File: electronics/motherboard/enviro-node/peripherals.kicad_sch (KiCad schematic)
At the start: 11 parts, among them J5 ST1W008S4AR1500, J6 2604-3105, Q3 BSS214NW, U3 TCA9534

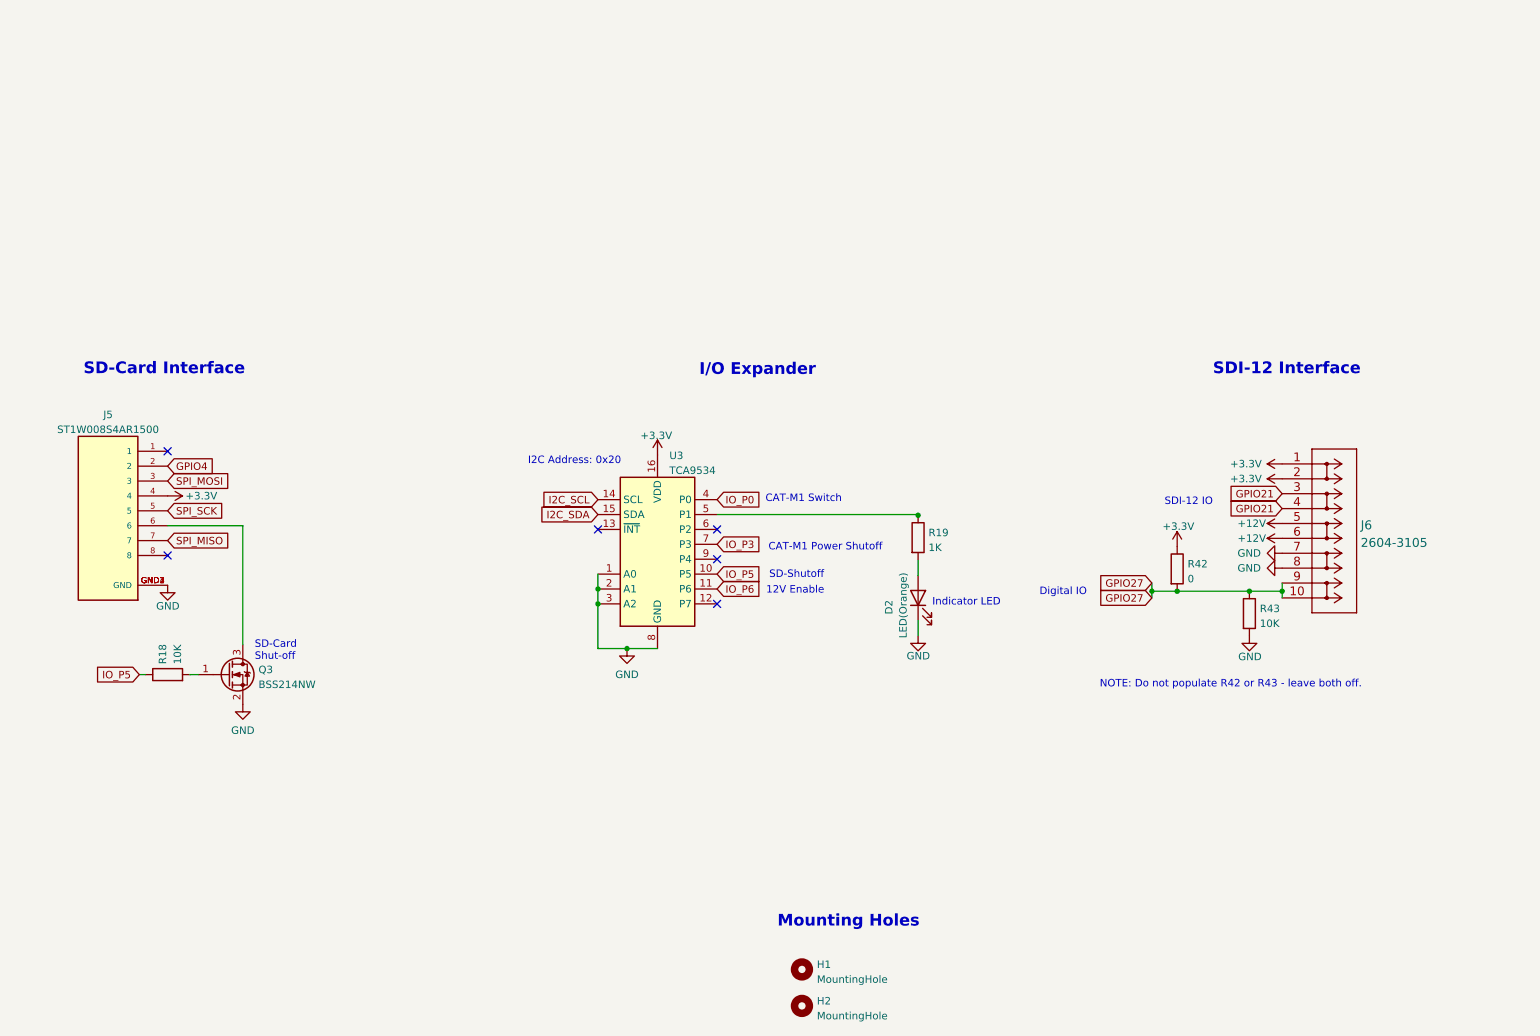
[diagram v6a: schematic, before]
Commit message: v1.0.3, added TMP1075 temp sensor, now using kicad 8.
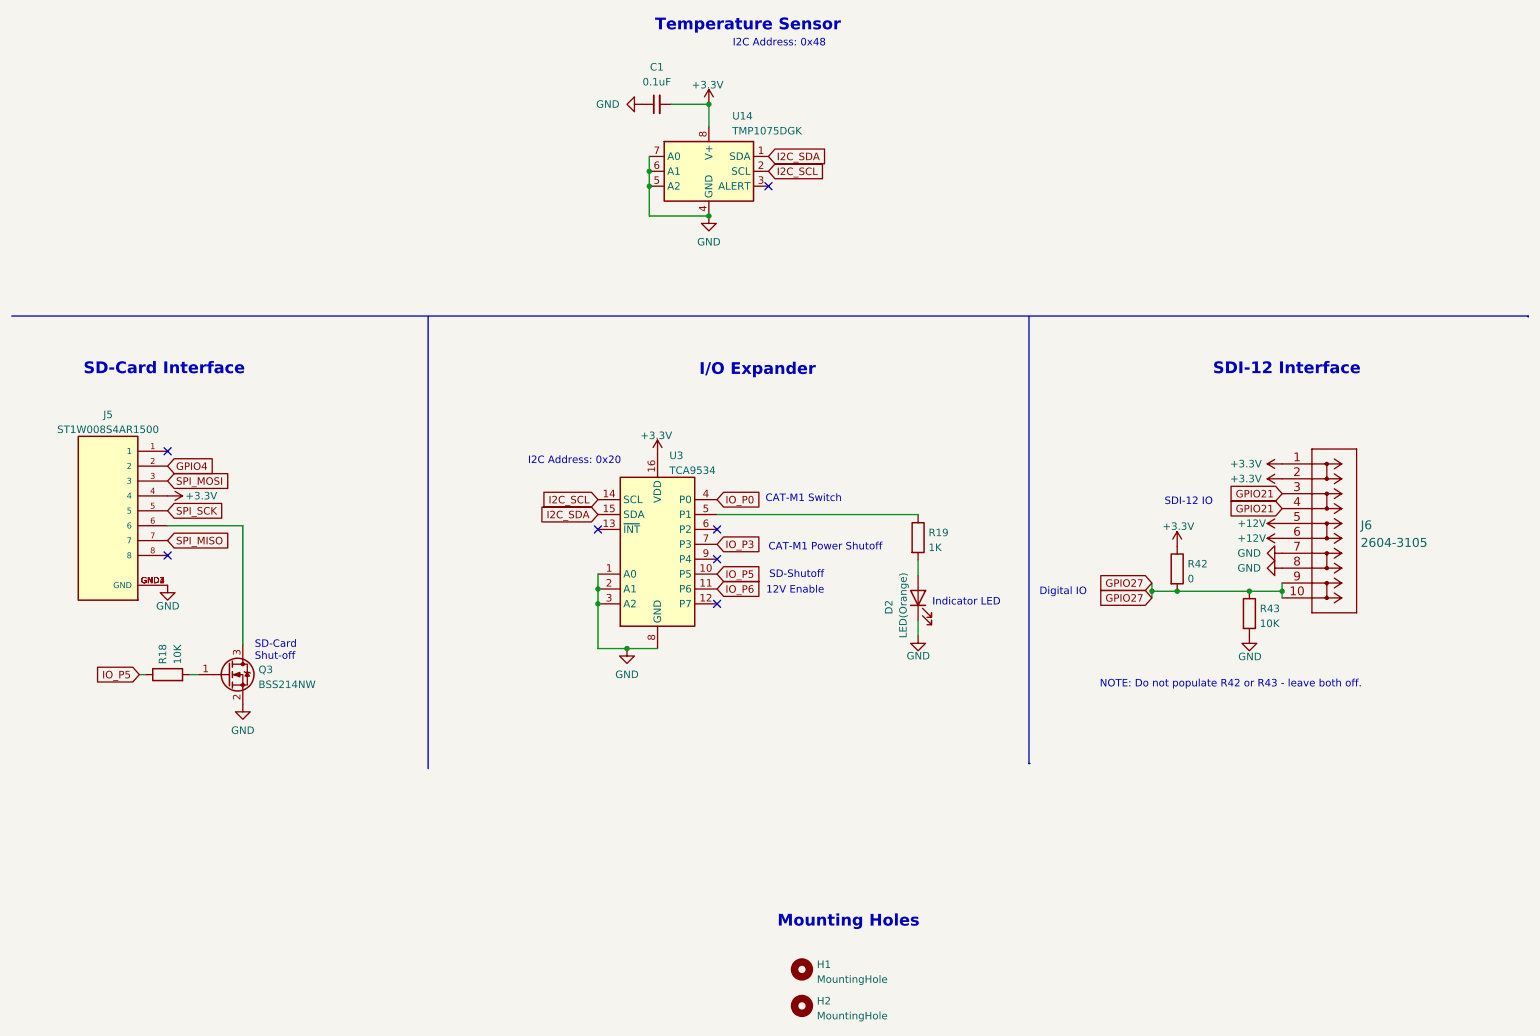
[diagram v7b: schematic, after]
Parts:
- added C1: 0.1uF, Capacitor_SMD:C_0805_2012Metric, symbol Device:C_Small
- added U14: TMP1075DGK, Package_SO:VSSOP-8_3.0x3.0mm_P0.65mm, symbol Sensor_Temperature:TMP1075DGK
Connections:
- net +3.3V: now also C1.2, U14.8 (V+)
- net GND: now also C1.1, U14.4 (GND), U14.5 (A2), U14.6 (A1), U14.7 (A0)
- net I2C_SCL: now also U14.2 (SCL)
- net I2C_SDA: now also U14.1 (SDA)
- no-connect marks 6 -> 7
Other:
- note added: "I2C Address: 0x48"
- note added: "Temperature Sensor"
